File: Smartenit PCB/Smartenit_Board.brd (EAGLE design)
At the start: 54.8 x 71.8 mm, 81 parts, among them J3 FTDI, Q1 QUARTZ_3.58M_2PIN, Q3 mmbt2222, Q4 mmbt2222, U1 ADE7953, U2 ESP-WROOM-32, U3 SN74LVC1G3157

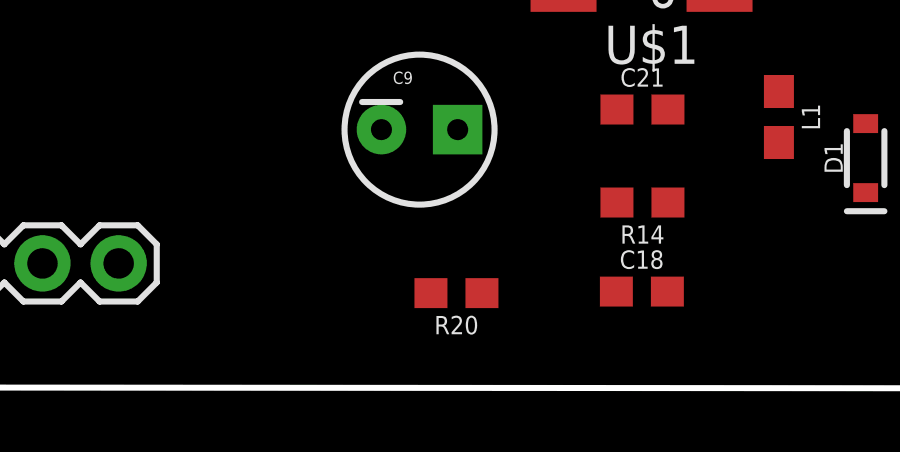
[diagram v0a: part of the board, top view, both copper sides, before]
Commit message: Update dimsension
updated dimensions and spacing for layout
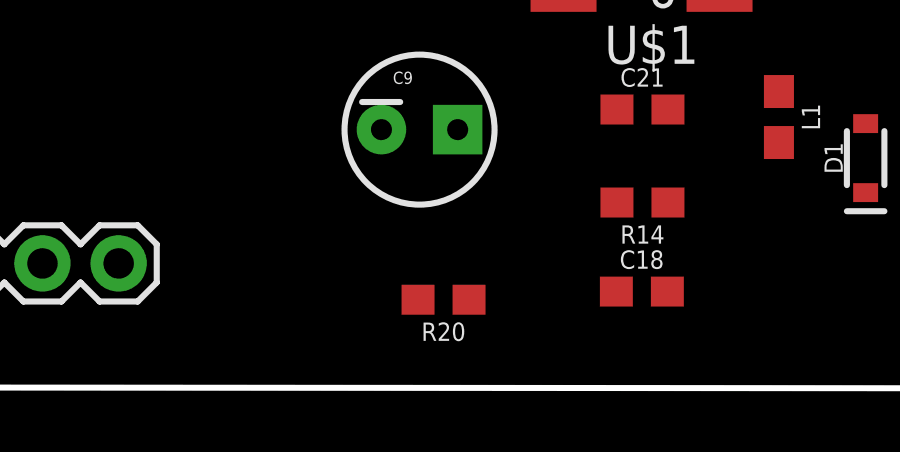
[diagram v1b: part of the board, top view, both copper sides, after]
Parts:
- moved R20 0.48 mm to (24.4, -39.9)
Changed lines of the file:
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@@
 <attribute name="PROD_ID" value="DIO-09646" x="38.42" y="-35.21" size="1.778" layer="27" rot="R90" display="off"/>
 </element>
-<element name="R20" library="SparkFun-Resistors" package="0603" value="100k" x="24.78" y="-39.71" rot="R180">
-<attribute name="PROD_ID" value="RES-07828" x="24.78" y="-39.71" size="1.778" layer="27" rot="R180" display="off"/>
+<element name="R20" library="SparkFun-Resistors" package="0603" value="100k" x="24.35" y="-39.93" rot="R180">
+<attribute name="PROD_ID" value="RES-07828" x="24.35" y="-39.93" size="1.778" layer="27" rot="R180" display="off"/>
 </element>
 <element name="Q2" library="semicon-smd-ipc" library_urn="urn:adsk.eagle:library:353" package="SOT23" package3d_urn="urn:adsk.eagle:package:26310/1" value="" x="45.06" y="-37.45" rot="R180"/>
@@
 <contactref element="J2" pad="6"/>
 <contactref element="R20" pad="2"/>
-<wire x1="23.93" y1="-39.71" x2="13.52" y2="-38.72" width="0" layer="19" extent="1-1"/>
+<wire x1="23.5" y1="-39.93" x2="13.52" y2="-38.72" width="0" layer="19" extent="1-1"/>
 </signal>
 <signal name="-12V">
@@
 <contactref element="R20" pad="1"/>
 <contactref element="Q2" pad="3"/>
-<wire x1="25.63" y1="-39.71" x2="45.06" y2="-38.55" width="0" layer="19" extent="1-1"/>
+<wire x1="25.2" y1="-39.93" x2="45.06" y2="-38.55" width="0" layer="19" extent="1-1"/>
 </signal>
 <signal name="DIO10">

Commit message: changes
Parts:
- removed D3: RED, SparkFun-LED:LED-0603
- removed D4: GREEN, SparkFun-LED:LED-0603
- removed Q3, Q4: mmbt2222, SparkFun:SOT23-3
- removed R37: 10K, microbuilder:_0603MP
- added C24: 104, Nizanlib:0402-CAP
- added C25: 104, SparkFun:0603-CAP
- added LD1: (no value), led:DUOLED-A-5MM
- added R38, R39, R41, R43: 470, Nizanlib:0402-RES
- added R40, R42: 12k, Nizanlib:0402-RES
- C23: value (none) -> 10uF/6.3V
- J3: value FTDI -> 2X5CONNECTOR1.27MM; device SparkFun-Connectors:1X06 -> Smart_Charger:1296-10
- R36: value 10K -> 12k; device microbuilder:0603-NO -> Nizanlib:0402-RES
- moved R36 124.6 mm to (-7.09, -96.6), turned to 0 degrees
- moved J3 12.8 mm to (32.9, 17.0)
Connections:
- removed net CTS: J3.2
- removed net DTR: J3.6, Q4.2, R36.1
- removed net EN: Q3.3, U2.3
- removed net GNDI: C1.1, C10.2, C11.1, C12.2, C13.1, C14.1, C15.1, C16.1, C17.2, C19.1, C2.1, C20.1, C3.1, C4.1, C5.1, C6.2, C7.2, C8.2, C9.2, D1.A, J1.2, J2.2, R1.1, R10.2, R11.2, R13.1, R15.1, R17.1, R18.2, R19.2, R2.2, R5.1, R6.2, R8.1, R9.1, S1.1, U$1.5, U1.14, U1.16, U1.4, U1.PAD
- removed net N$31: U2.34
- removed net N$56: Q3.1, R36.2
- removed net N$57: J3.3
- removed net N$58: Q4.1, R37.2
- removed net RTS: Q3.2, R37.1
- removed net RX: J3.5
- removed net TX: J3.4
- new net N$40: J3.3, R41.2
- new net N$62: J3.2, R39.1
- new net N$65: J3.8, R38.1
- new net NRST: C24.2, R39.2, R40.1, U2.3
- new net RXD0: R38.2, U2.34
- new net TXD0: J3.7, U2.35
- net 3.3V: now also C25.1, J3.4, LD1.A, R40.2, R42.2, R43.1; no longer D3.A, D4.A
- net GND: now also C1.1, C10.2, C11.1, C12.2, C13.1, C14.1, C15.1, C16.1, C17.2, C19.1, C2.1, C20.1, C24.1, C25.2, C3.1, C4.1, C5.1, C6.2, C7.2, C8.2, C9.2, D1.A, J1.2, J2.2, J3.10, R1.1, R10.2, R11.2, R13.1, R15.1, R17.1, R18.2, R19.2, R2.2, R36.1, R5.1, R6.2, R8.1, R9.1, S1.1, U$1.5, U1.14, U1.16, U1.4, U1.PAD; no longer J3.1
- net GPIO0: now also R41.1, R42.1; no longer Q4.3
- net N$25: now also LD1.CX; no longer D3.C
- net N$26: now also LD1.CR; no longer D4.C
- net N$30: now also R43.2, U2.24; no longer U2.35
- net SS: now also R36.2
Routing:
- net GNDI: track 6.56 -> 0.00 mm
- net GND: track 0.00 -> 6.56 mm

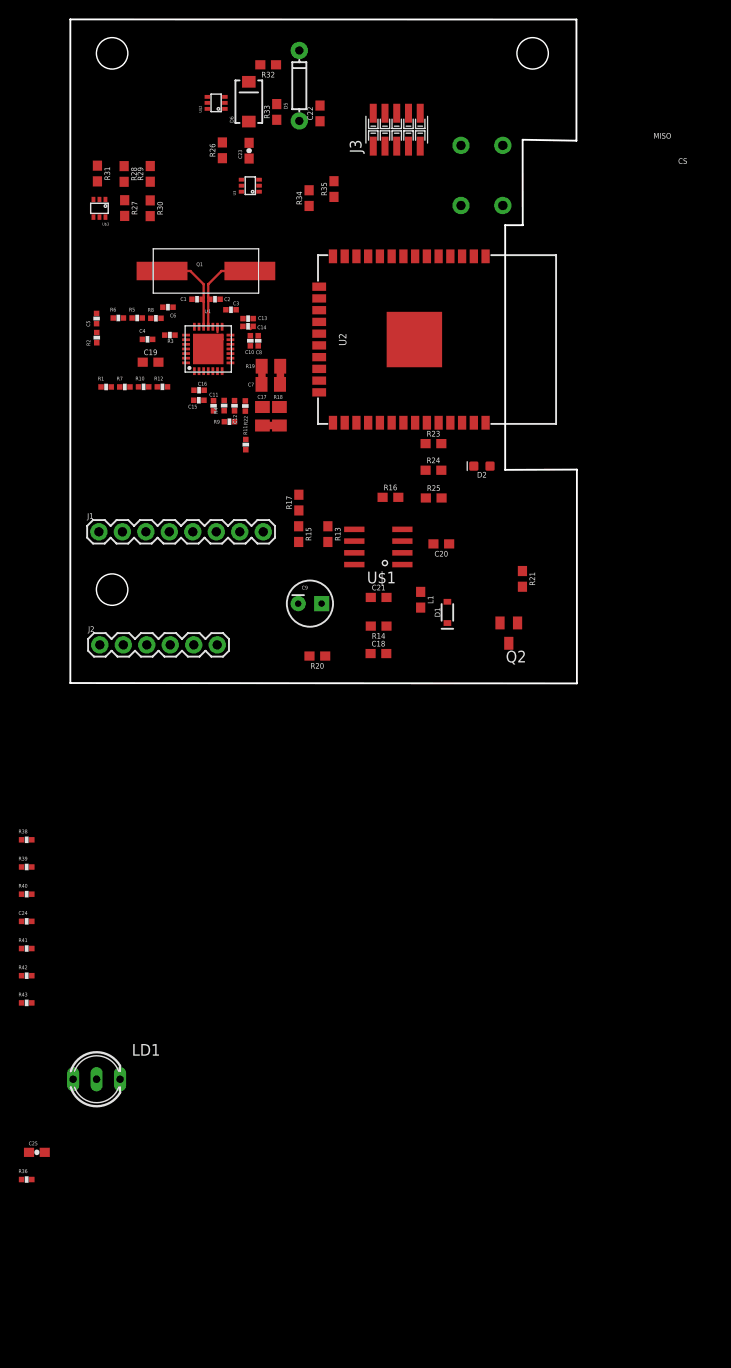
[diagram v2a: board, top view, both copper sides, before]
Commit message: Updated schematic dimensions
dimensions and interspacing between holes LEDs and pin headers
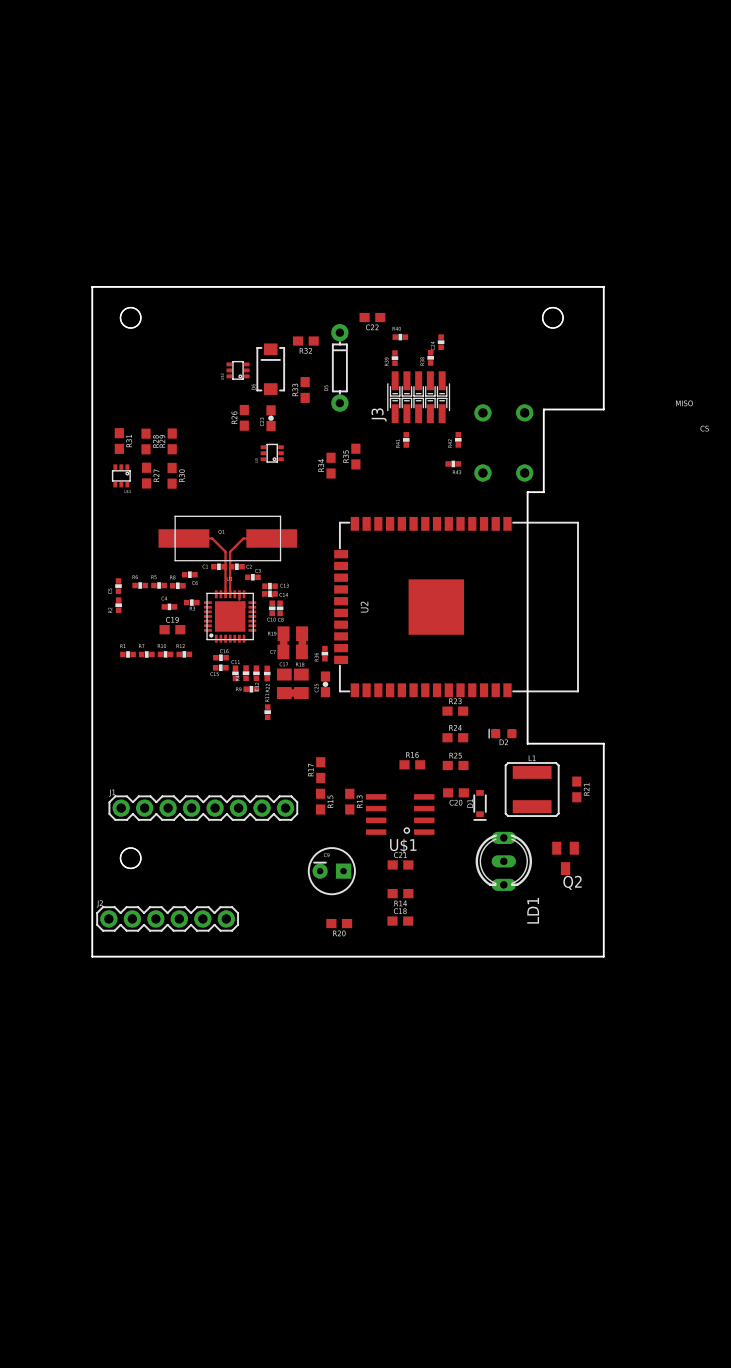
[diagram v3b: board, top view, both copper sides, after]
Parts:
- L1: value 33nH/±5%/500mA -> 47µH/±30%/750mA; device SparkFun-Coils:0603 -> SparkFun-Coils:CR54
- moved C24 77.0 mm to (37.7, -5.98), turned to 90 degrees
- moved R42 74.4 mm to (39.6, -16.5), turned to 90 degrees
- moved R43 74.4 mm to (39.1, -19.1), turned to 180 degrees
- moved R40 72.6 mm to (33.3, -5.43)
- moved R41 68.7 mm to (34.0, -16.6), turned to 90 degrees
- moved R38 68.0 mm to (36.6, -7.67), turned to 90 degrees
- moved R39 68.0 mm to (32.8, -7.70), turned to 90 degrees
- moved R36 65.4 mm to (25.2, -39.7), turned to 90 degrees
- moved C25 59.5 mm to (25.2, -43.0), turned to 90 degrees
- moved LD1 50.0 mm to (44.5, -62.1), turned to 270 degrees
- moved D5 30.8 mm to (26.8, -8.76)
- moved R33 30.2 mm to (23.0, -11.2)
- moved R32 30.2 mm to (23.1, -5.85)
- moved J1 30.0 mm to (3.13, -56.4)
- moved J2 29.7 mm to (1.80, -68.4)
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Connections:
- net 3.3V: now also L1.P$1; no longer L1.1
- net N$18: now also L1.P$2; no longer L1.2
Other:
- board size 54.8 x 71.8 mm -> 55.3 x 72.5 mm
